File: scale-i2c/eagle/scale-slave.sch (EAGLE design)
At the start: 41 parts, among them CON1 SPI, IC1 MCP1703CB, J2 RJ12RIGHTANGLE-I2C, J3 RJ12RIGHTANGLE-I2C, U1 ATMEGA328P_TQFP, U2 HX711, X1 8MHz

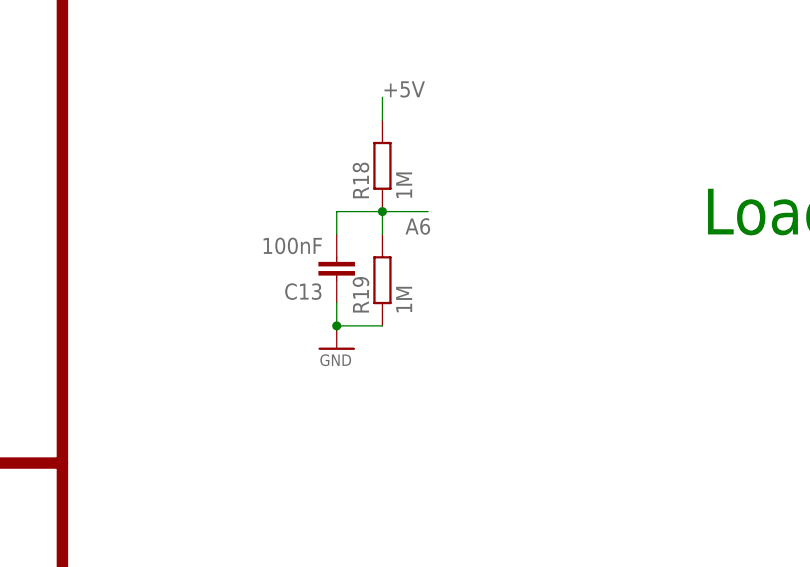
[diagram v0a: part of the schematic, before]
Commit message: correct resistor for voltage check
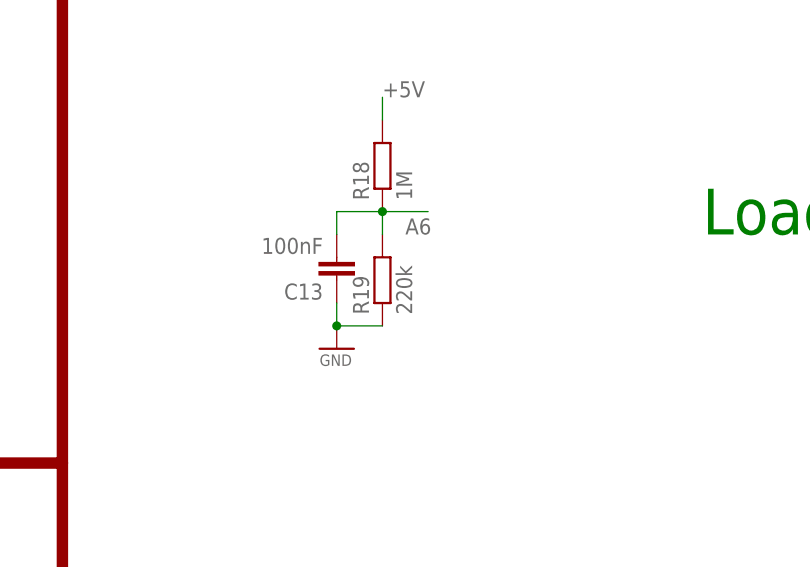
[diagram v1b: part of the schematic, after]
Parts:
- R19: value 1M -> 220k
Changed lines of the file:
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@@
 <attribute name="LCSC" value="C17514"/>
 </part>
-<part name="R19" library="rcl" deviceset="R-EU_" device="R0805" value="1M">
+<part name="R19" library="rcl" deviceset="R-EU_" device="R0805" value="220k">
 <attribute name="ELECROW" value="C17514"/>
 <attribute name="LCSC" value="C17514"/>
